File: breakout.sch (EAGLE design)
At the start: 21 parts, among them IC2 REG1117, Y1 12mhz

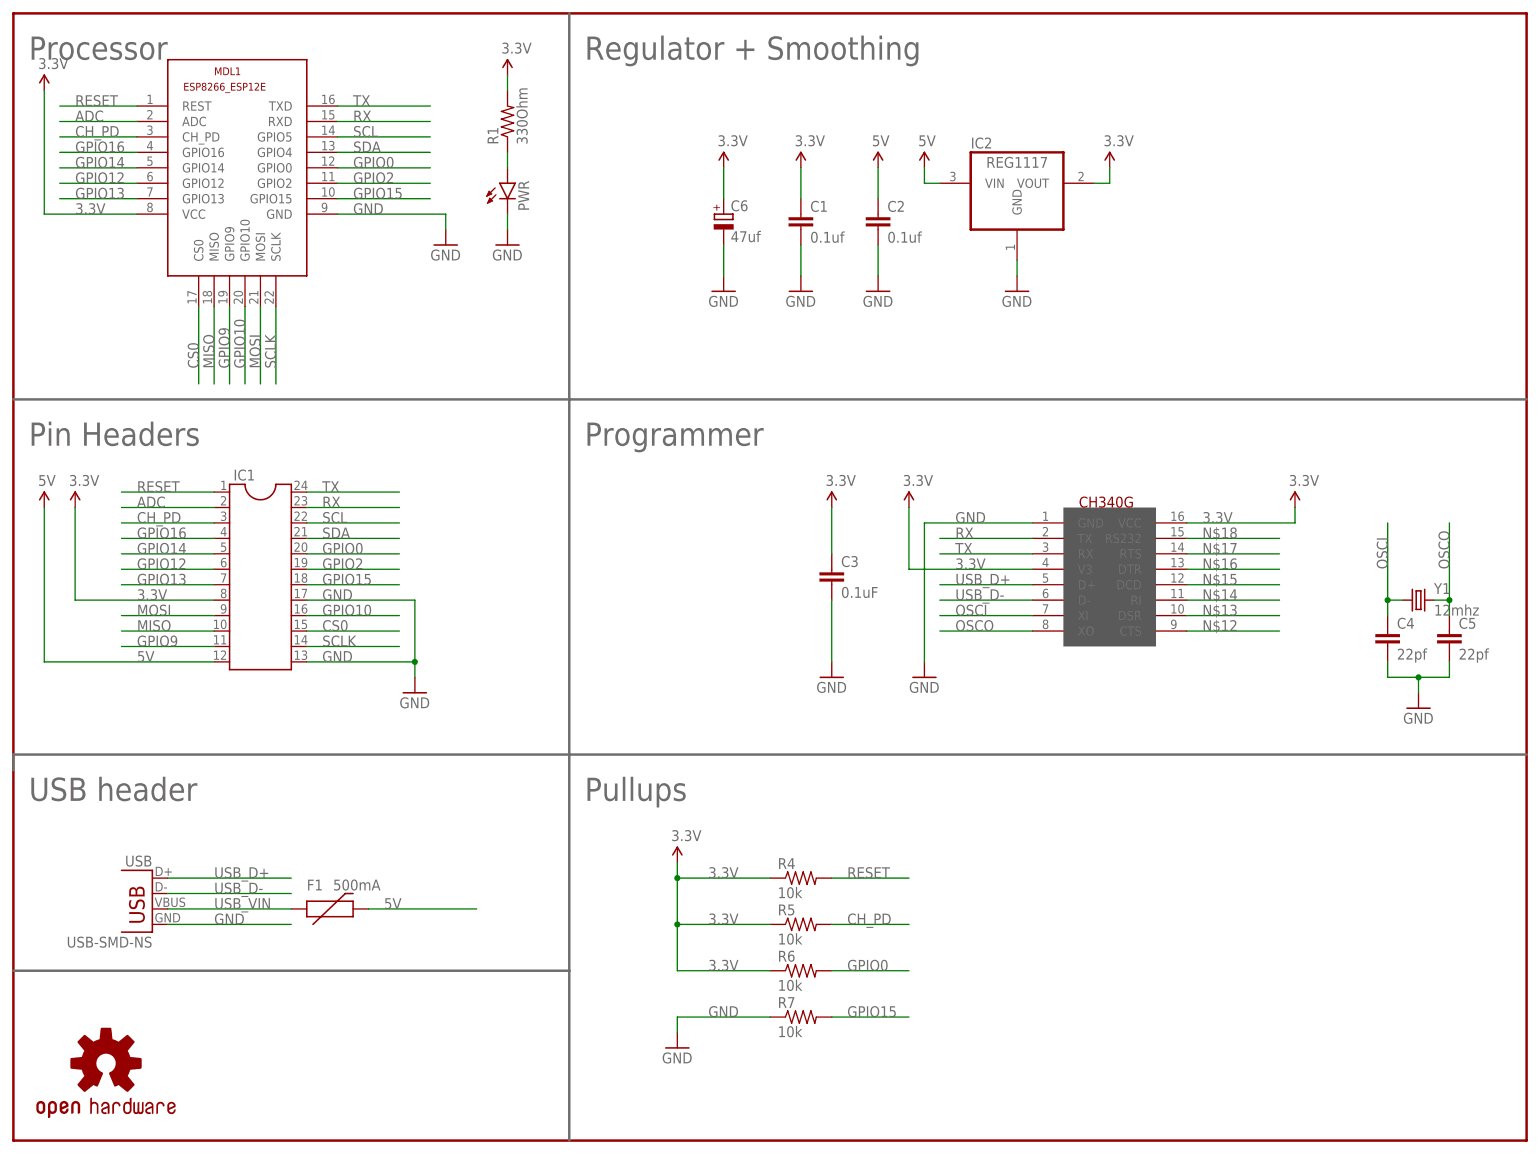
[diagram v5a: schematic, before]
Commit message: Added TX/RX LEDs. Aww yiss.
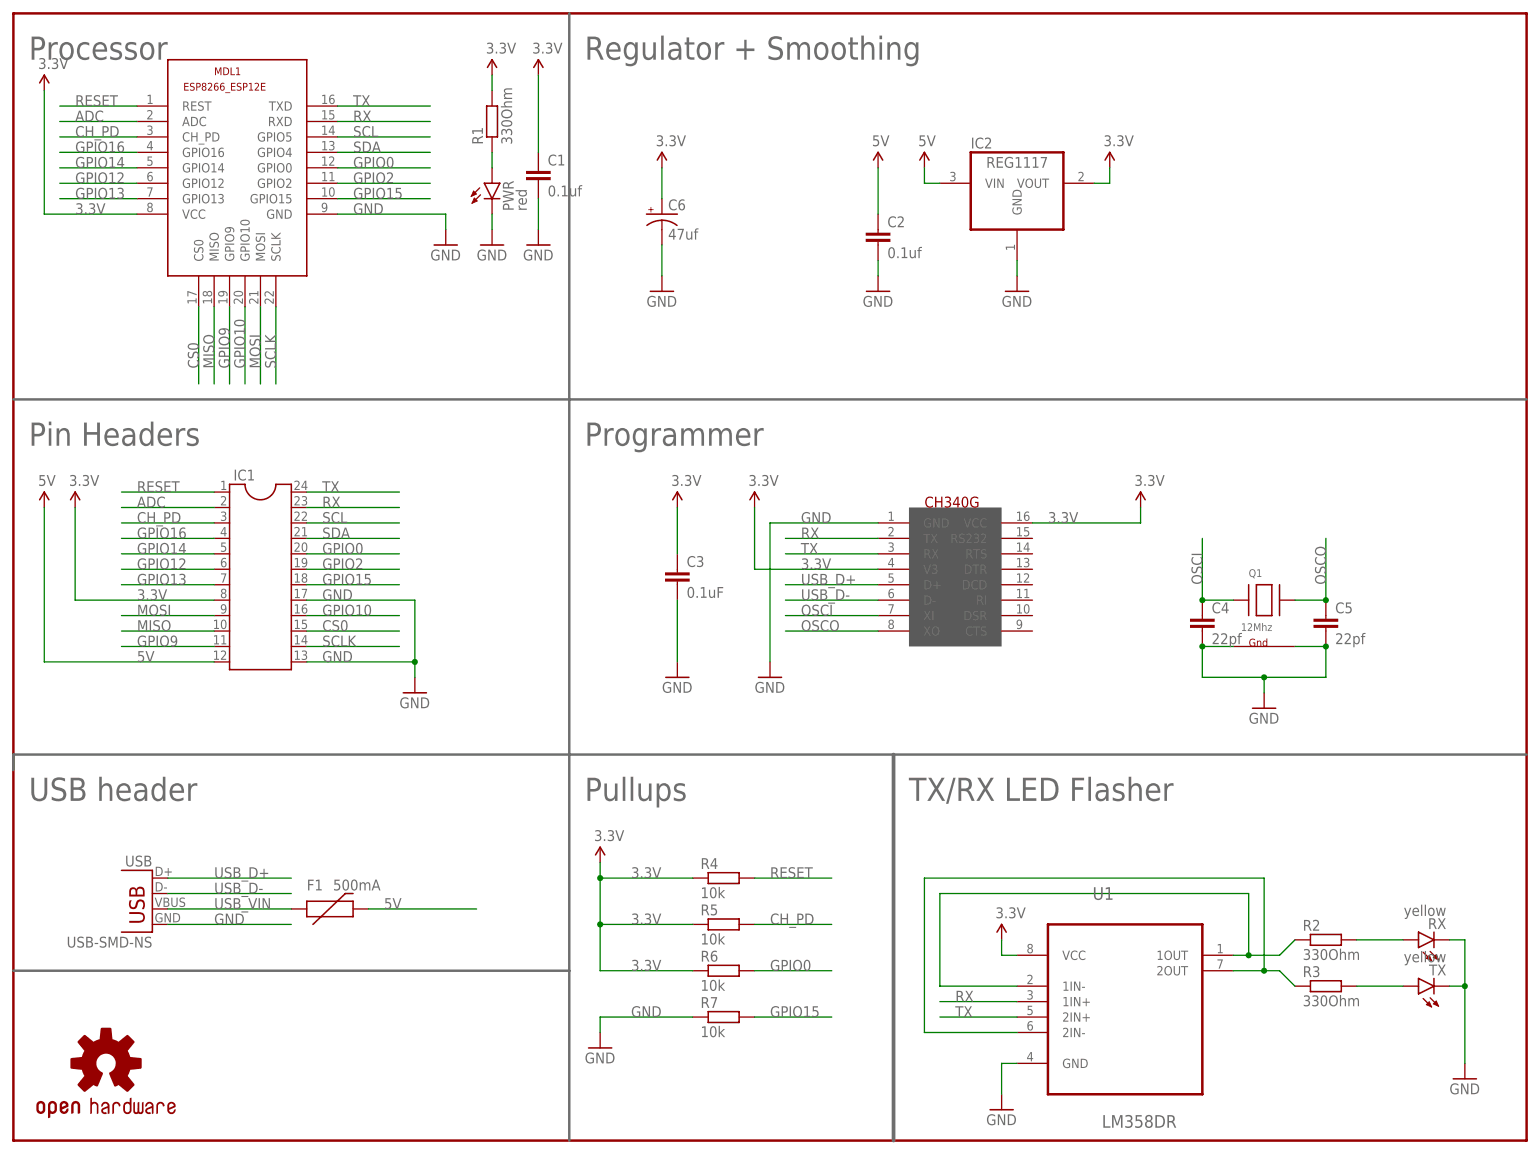
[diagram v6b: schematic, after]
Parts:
- removed Y1: 12mhz, SparkFun-FreqCtrl:CRYSTALSMD
- added Q1: 12Mhz, adafruit:XTAL-4-3225
- added R2, R3: 330Ohm, rcl:R-EU_R0805
- added RX, TX: yellow, SparkFun-LED:LED0603
- added U1: LM358DR, Texas Instruments_By_element14_Batch_1:LM358DR
- C1, C2, C4, C5: device SparkFun-Capacitors:CAP1206 -> rcl:C-EUC0805
- C3: device rcl:C-EUC1206K -> rcl:C-EUC0805
- C6: device rcl:CPOL-EUSMCB -> SparkFun:CAP_POLC
- PWR: value (none) -> red; device SparkFun-LED:LED1206 -> SparkFun-LED:LED0603
- R1, R4, R5, R6, R7: device SparkFun-Resistors:RESISTOR1206 -> rcl:R-EU_R0805
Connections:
- removed net N$12: U$1.CTS
- removed net N$13: U$1.DSR
- removed net N$14: U$1.RI
- removed net N$15: U$1.DCD
- removed net N$16: U$1.DTR
- removed net N$17: U$1.RTS
- removed net N$18: U$1.RS232
- new net N$2: R3.2, TX.A
- new net N$3: R2.1, U1.1IN-, U1.1OUT
- new net N$4: R3.1, U1.2IN-, U1.2OUT
- new net N$5: R2.2, RX.A
- net 3.3V: now also U1.VCC
- net GND: now also Q1.G1, Q1.G2, RX.C, TX.C, U1.GND
- net OSCI: now also Q1.X1; no longer Y1.1
- net OSCO: now also Q1.X2; no longer Y1.2
- net RX: now also U1.1IN+
- net TX: now also U1.2IN+
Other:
- note added: "TX/RX LED Flasher"
- moved on the sheet: C1, C2, C3, C4, C5, C6, PWR

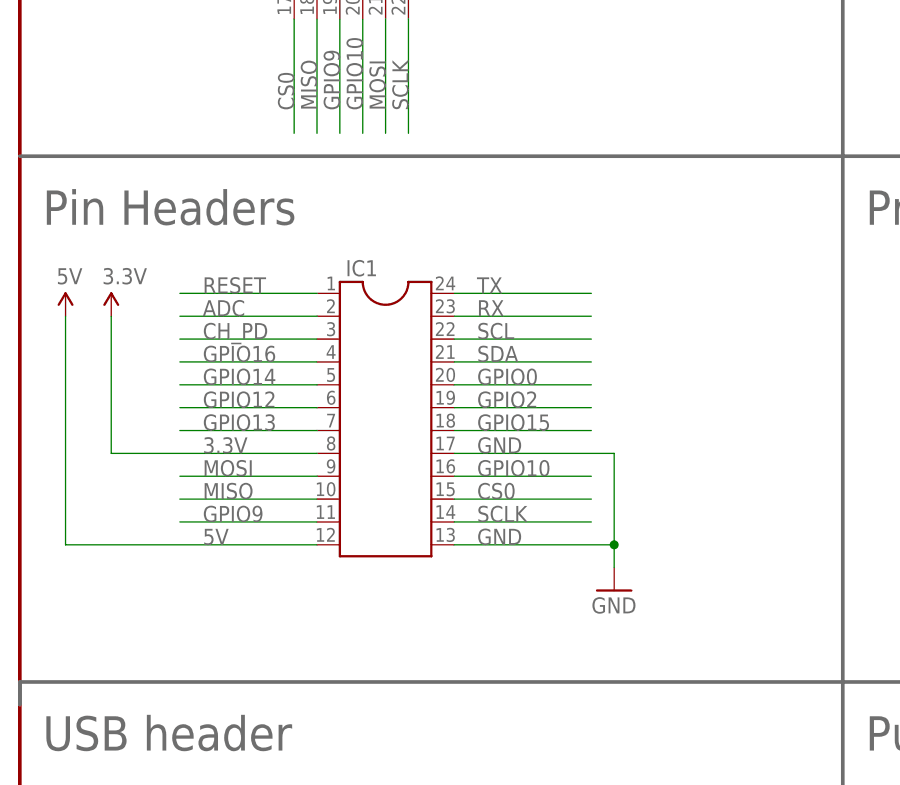
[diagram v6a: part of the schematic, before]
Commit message: Rounded corners + notch.
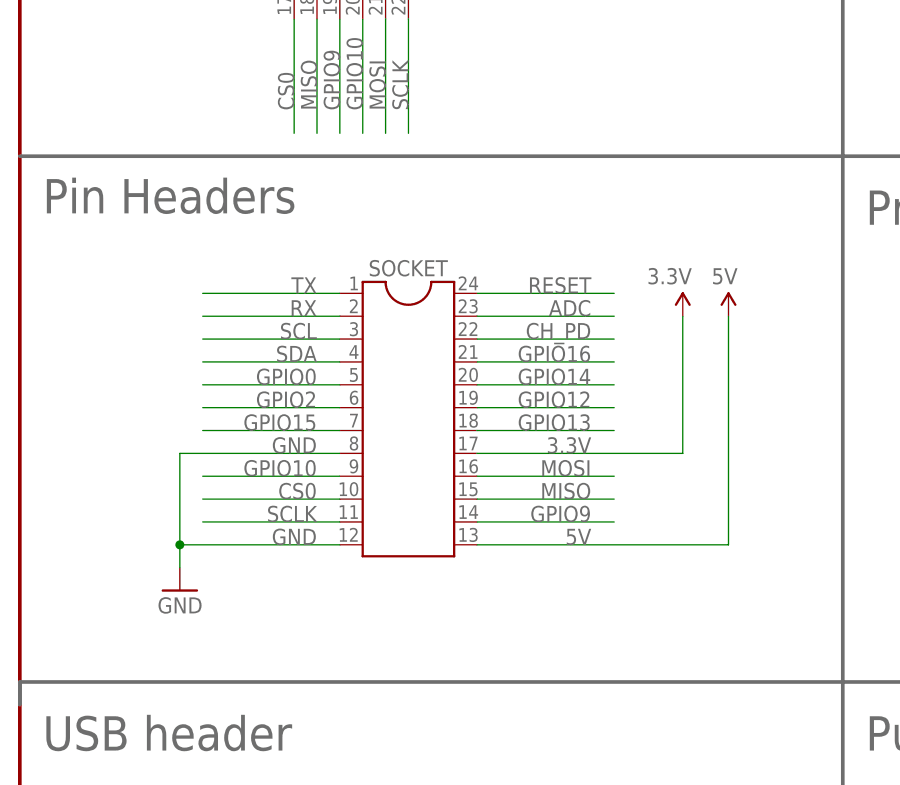
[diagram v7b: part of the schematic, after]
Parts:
- removed IC1: (no value), ic-package:DIL24-9
- added SOCKET: (no value), ic-package:DIL24-9
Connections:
- net 3.3V: now also SOCKET.17; no longer IC1.8
- net 5V: now also SOCKET.13; no longer IC1.12
- net ADC: now also SOCKET.23; no longer IC1.2
- net CH_PD: now also SOCKET.22; no longer IC1.3
- net CS0: now also SOCKET.10; no longer IC1.15
- net GND: now also SOCKET.12, SOCKET.8; no longer IC1.13, IC1.17
- net GPIO0: now also SOCKET.5; no longer IC1.20
- net GPIO10: now also SOCKET.9; no longer IC1.16
- net GPIO12: now also SOCKET.19; no longer IC1.6
- net GPIO13: now also SOCKET.18; no longer IC1.7
- net GPIO14: now also SOCKET.20; no longer IC1.5
- net GPIO15: now also SOCKET.7; no longer IC1.18
- net GPIO16: now also SOCKET.21; no longer IC1.4
- net GPIO2: now also SOCKET.6; no longer IC1.19
- net GPIO9: now also SOCKET.14; no longer IC1.11
- net MISO: now also SOCKET.15; no longer IC1.10
- net MOSI: now also SOCKET.16; no longer IC1.9
- net RESET: now also SOCKET.24; no longer IC1.1
- net RX: now also SOCKET.2; no longer IC1.23
- net SCL: now also SOCKET.3; no longer IC1.22
- net SCLK: now also SOCKET.11; no longer IC1.14
- net SDA: now also SOCKET.4; no longer IC1.21
- net TX: now also SOCKET.1; no longer IC1.24
